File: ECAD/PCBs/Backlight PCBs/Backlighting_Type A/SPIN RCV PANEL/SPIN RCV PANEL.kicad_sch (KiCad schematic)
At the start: 86 parts, among them J1 Conn_01x04_Female, J2 Conn_01x04_Female

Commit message: Drawing Sheet & Silkscreen update - Backlight Panels (Fc thru Spin)
1:  Updated/Relinked Drawing Sheet for both PCB and Schematics
2:  Standardized Silkscreen (if required)

Finished Remaining Backlighting Type A & Type B PCBs.....
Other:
- title: (none) -> SPIN RCV PANEL
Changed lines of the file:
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@@
 (kicad_sch (version 20211123) (generator eeschema)
   (paper "A4")
+  (title_block
+    (title "SPIN RCV PANEL")
+    (date "2023-02-10")
+    (rev "3")
+  )
   (junction (at 195.58 104.14) (diameter 0) (color 0 0 0 0)
   )

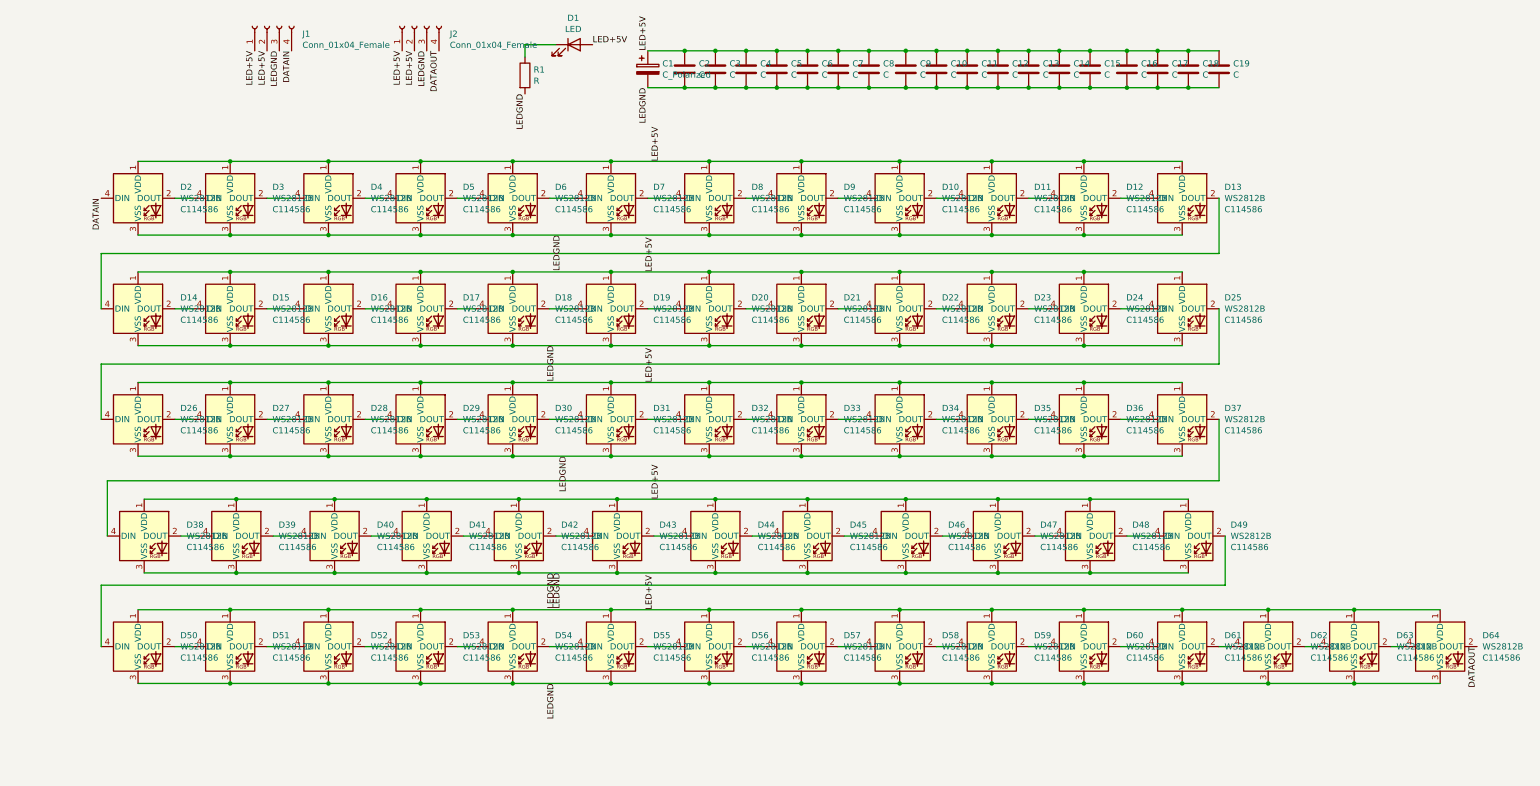
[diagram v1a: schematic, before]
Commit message: KiCad 7 Transition - SPIN RCV Panel
PCB and Schematic standardization
Updated silkscreen text
AddedTestpoints
Recompiled assets and manufacturing files

Fixed a previous error - The footprints for a few WS2812B's were swapped for WS2812B-Mini's and visa versa due to reference designators being mismatched.  It was done in a previous version of the PCB's that I had transitioned.  The LED's have been reverted back to their original footprints based on the latest PCB in the Master branch.

Traces have been updated and fixed to allow better connectivity
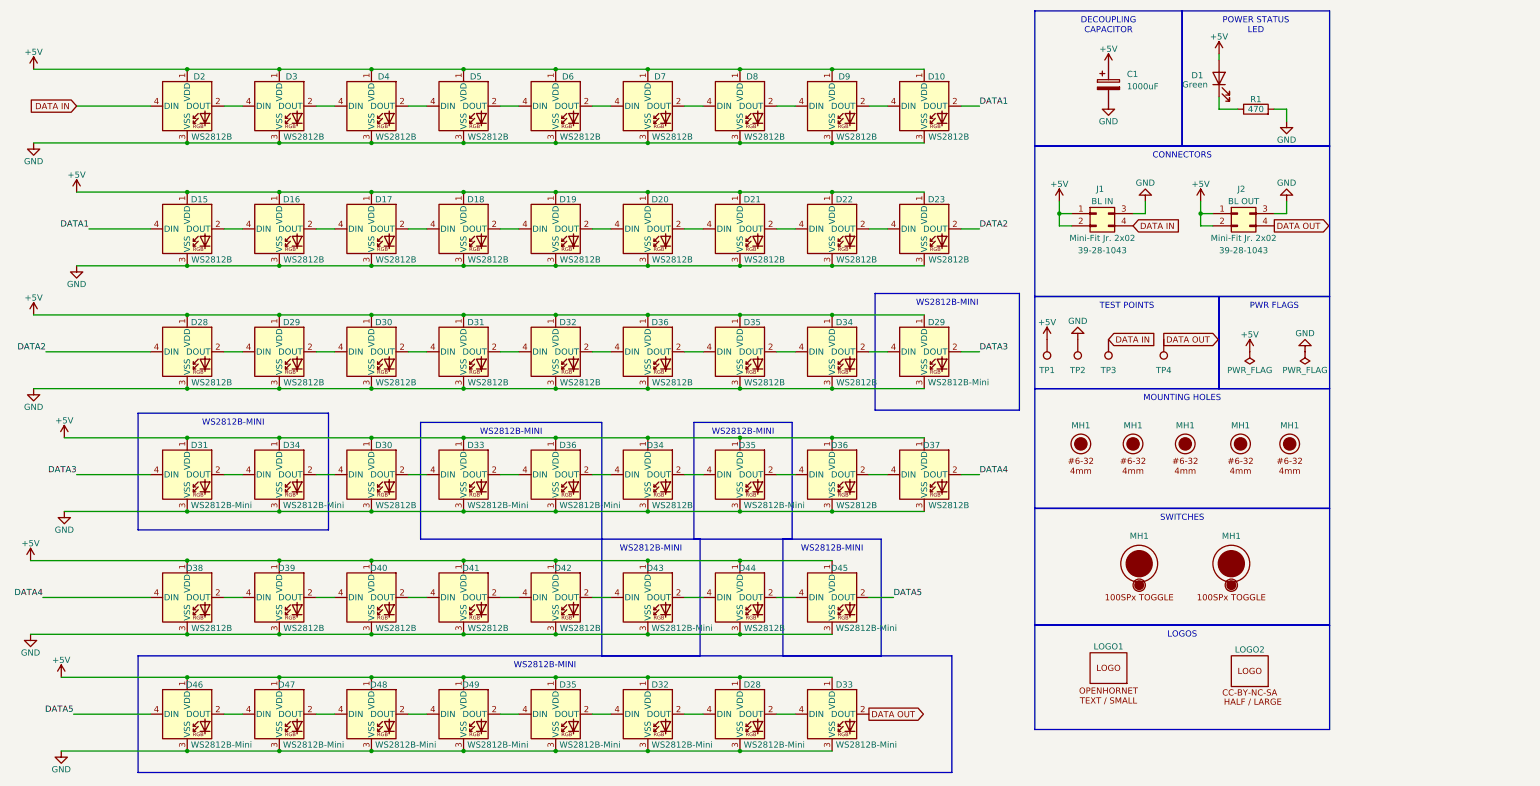
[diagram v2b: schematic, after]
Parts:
- removed C1: C_Polarized, OH_Footprints:CP_Elec_8x10, symbol Device:C_Polarized
- removed C10, C11, C12, C13, C14, C15, C16, C17, C18, C19, C2, C3, C4, C5, C6, C7, C8, C9: C, OH_Footprints:C_0603_1608Metric, symbol Device:C
- removed D1: LED, OH_Footprints:LED_D3.0mm, symbol Device:LED
- removed D10, D11, D12, D13, D14, D15, D16, D17, D18, D19, D2, D20, D21, D22, D23, D24, D26, D27, D28, D3, D31, D38, D4, D41, D42, D43, D46, D47, D48, D5, D50, D52, D54, D55, D56, D57, D58, D59, D6, D60, D61, D62, D63, D64, D7, D8, D9: WS2812B, OH_Footprints:LED_WS2812B_PLCC4_5.0x5.0mm_P3.2mm, symbol LED:WS2812B
- removed D25, D29, D30, D32, D33, D34, D35, D36, D37, D39, D40, D44, D45, D49, D51, D53: WS2812B, OH_Footprints:LED_WS2812B-MINI_PLCC4_3.5x3.5mm_P1.75mm, symbol LED:WS2812B
- removed J1, J2: Conn_01x04_Female, OH_Footprints:Molex_Mini-Fit_Jr_5566-04A_2x02_P4.20mm_Vertical, symbol Connector:Conn_01x04_Female
- removed R1: R, OH_Footprints:R_0603_1608Metric, symbol Device:R
- added C1: 1000uF, OH_Footprints:CP_Elec_8x10, symbol OH_Symbols:Capacitor_Polarized_8x10_1000uF
- added D1: Green, OH_Footprints:LED_D3.0mm, symbol OH_Symbols:LED_3.0mm_Green
- added D10, D15, D16, D17, D18, D19, D2, D20, D21, D22, D23, D28, D29, D3, D30 (x2), D31, D32, D34 (x2), D35, D36 (x2), D37, D38, D39, D4, D40, D41, D42, D44, D5, D6, D7, D8, D9: WS2812B, OH_Footprints:LED_WS2812B_PLCC4_5.0x5.0mm_P3.2mm, symbol OH_Symbols:WS2812B
- added D28, D29, D31, D32, D33 (x2), D34, D35 (x2), D36, D43, D45, D46, D47, D48, D49: WS2812B-Mini, OH_Footprints:LED_WS2812B-MINI_PLCC4_3.5x3.5mm_P1.75mm, symbol OH_Symbols:WS2812B-Mini
- added J1, J2: Mini-Fit Jr. 2x02, OH_Footprints:Molex_Mini-Fit_Jr_5566-04A_2x02_P4.20mm_Vertical, symbol OH_Symbols:Molex_Mini-Fit_Jr._2x02
- added LOGO1: LOGO, OH_Footprints:LOGO_OH_Text_Small, symbol OH_Symbols:LOGO_OpenHornet_Text_Small
- added LOGO2: LOGO, OH_Footprints:LOGO_CC-BY-NC-SA_Half_Large, symbol OH_Symbols:LOGO_License_Half_Large
- added MH1 (x5): 6x32 / 4mm, OH_Footprints:MountingHole_6-32_PHS, symbol OH_Symbols:MountingHole_6x32_PHS
- added MH1 (x2): Switch_100SPx, OH_Footprints:100SPX_Toggle_13mm_x_18mm, symbol OH_Symbols:MountingHole_100SPx_Toggle
- added R1: 470, OH_Footprints:R_0603_1608Metric, symbol OH_Symbols:Resistor_0603_470Ω
- added TP1, TP2, TP3, TP4: TestPoint, OH_Footprints:TestPoint_THTPad_D1.5mm_Drill0.7mm, symbol OH_Symbols:TestPoint
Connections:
- new net: D43.2 (DOUT), D44.4 (DIN)
- new net: D42.2 (DOUT), D43.4 (DIN)
- new net: D31.2 (DOUT), D34.4 (DIN)
- new net: D29.4 (DIN), D34.2 (DOUT)
- new net: D36.2 (DOUT), D37.4 (DIN)
- new net: D35.2 (DOUT), D36.4 (DIN)
- new net: D4.2 (DOUT), D5.4 (DIN)
- new net: D3.2 (DOUT), D4.4 (DIN)
- new net: D41.2 (DOUT), D42.4 (DIN)
- new net: D40.2 (DOUT), D41.4 (DIN)
- new net: D22.2 (DOUT), D23.4 (DIN)
- new net: D21.2 (DOUT), D22.4 (DIN)
- new net: D1.1 (K), R1.1
- new net: D39.2 (DOUT), D40.4 (DIN)
- new net: D46.2 (DOUT), D47.4 (DIN)
- new net: D35.4 (DIN), D49.2 (DOUT)
- new net: D48.2 (DOUT), D49.4 (DIN)
- new net: D2.2 (DOUT), D3.4 (DIN)
- new net: D10.4 (DIN), D9.2 (DOUT)
- new net: D38.2 (DOUT), D39.4 (DIN)
- new net: D15.2 (DOUT), D16.4 (DIN)
- new net: D28.4 (DIN), D32.2 (DOUT)
- new net: D32.4 (DIN), D35.2 (DOUT)
- new net: D18.2 (DOUT), D19.4 (DIN)
- new net: D17.2 (DOUT), D18.4 (DIN)
- new net: D20.2 (DOUT), D21.4 (DIN)
- new net: D34.4 (DIN), D35.2 (DOUT)
- new net: D35.4 (DIN), D36.2 (DOUT)
- new net: D19.2 (DOUT), D20.4 (DIN)
- new net: D30.2 (DOUT), D33.4 (DIN)
- new net: D30.4 (DIN), D34.2 (DOUT)
- new net: D47.2 (DOUT), D48.4 (DIN)
- new net: D34.4 (DIN), D36.2 (DOUT)
- new net: D33.2 (DOUT), D36.4 (DIN)
- new net: D34.2 (DOUT), D35.4 (DIN)
- new net: D16.2 (DOUT), D17.4 (DIN)
- new net: D32.2 (DOUT), D36.4 (DIN)
- new net: D31.2 (DOUT), D32.4 (DIN)
- new net: D30.2 (DOUT), D31.4 (DIN)
- new net: D44.2 (DOUT), D45.4 (DIN)
- new net: D8.2 (DOUT), D9.4 (DIN)
- new net: D7.2 (DOUT), D8.4 (DIN)
- new net: D6.2 (DOUT), D7.4 (DIN)
- new net: D28.2 (DOUT), D29.4 (DIN)
- new net: D5.2 (DOUT), D6.4 (DIN)
- new net: D29.2 (DOUT), D30.4 (DIN)
- new net: D28.2 (DOUT), D33.4 (DIN)
- new net +5V: C1.1, D1.2 (A), D10.1 (VDD), D15.1 (VDD), D16.1 (VDD), D17.1 (VDD), D18.1 (VDD), D19.1 (VDD), D2.1 (VDD), D20.1 (VDD), D21.1 (VDD), D22.1 (VDD), D23.1 (VDD), D28.1 (VDD), D28.1 (VDD), D29.1 (VDD), D29.1 (VDD), D3.1 (VDD), D30.1 (VDD), D30.1 (VDD), D31.1 (VDD), D31.1 (VDD), D32.1 (VDD), D32.1 (VDD), D33.1 (VDD), D33.1 (VDD), D34.1 (VDD), D34.1 (VDD), D34.1 (VDD), D35.1 (VDD), D35.1 (VDD), D35.1 (VDD), D36.1 (VDD), D36.1 (VDD), D36.1 (VDD), D37.1 (VDD), D38.1 (VDD), D39.1 (VDD), D4.1 (VDD), D40.1 (VDD), D41.1 (VDD), D42.1 (VDD), D43.1 (VDD), D44.1 (VDD), D45.1 (VDD), D46.1 (VDD), D47.1 (VDD), D48.1 (VDD), D49.1 (VDD), D5.1 (VDD), D6.1 (VDD), D7.1 (VDD), D8.1 (VDD), D9.1 (VDD), J1.1 (Pin_1), J1.2 (Pin_3), J2.1 (Pin_1), J2.2 (Pin_3), TP1.1
- new net DATA IN: D2.4 (DIN), J1.4 (Pin_4), TP3.1
- new net DATA OUT: D33.2 (DOUT), J2.4 (Pin_4), TP4.1
- new net DATA1: D10.2 (DOUT), D15.4 (DIN)
- new net DATA2: D23.2 (DOUT), D28.4 (DIN)
- new net DATA3: D29.2 (DOUT), D31.4 (DIN)
- new net DATA4: D37.2 (DOUT), D38.4 (DIN)
- new net DATA5: D45.2 (DOUT), D46.4 (DIN)
- new net GND: C1.2, D10.3 (VSS), D15.3 (VSS), D16.3 (VSS), D17.3 (VSS), D18.3 (VSS), D19.3 (VSS), D2.3 (VSS), D20.3 (VSS), D21.3 (VSS), D22.3 (VSS), D23.3 (VSS), D28.3 (VSS), D28.3 (VSS), D29.3 (VSS), D29.3 (VSS), D3.3 (VSS), D30.3 (VSS), D30.3 (VSS), D31.3 (VSS), D31.3 (VSS), D32.3 (VSS), D32.3 (VSS), D33.3 (VSS), D33.3 (VSS), D34.3 (VSS), D34.3 (VSS), D34.3 (VSS), D35.3 (VSS), D35.3 (VSS), D35.3 (VSS), D36.3 (VSS), D36.3 (VSS), D36.3 (VSS), D37.3 (VSS), D38.3 (VSS), D39.3 (VSS), D4.3 (VSS), D40.3 (VSS), D41.3 (VSS), D42.3 (VSS), D43.3 (VSS), D44.3 (VSS), D45.3 (VSS), D46.3 (VSS), D47.3 (VSS), D48.3 (VSS), D49.3 (VSS), D5.3 (VSS), D6.3 (VSS), D7.3 (VSS), D8.3 (VSS), D9.3 (VSS), J1.3 (Pin_2), J2.3 (Pin_2), R1.2, TP2.1
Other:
- company: (none) -> www.openhornet.comm
